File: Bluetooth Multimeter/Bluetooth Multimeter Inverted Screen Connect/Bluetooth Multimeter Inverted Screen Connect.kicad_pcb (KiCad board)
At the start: 2 copper layers, 55 x 90 mm, 33 parts, among them J1 V/Ohm, J2 Com, J3 mA, J4 A, J5 Parallel Prot, J6 3.3V, J7 GND, K1 Low Range, K2 Medium Range, K3 High Range, K4 UH Range (Ohm Only), K5 V/Ohm Switch, U1 ItsyBitsy_NRF52840_Big

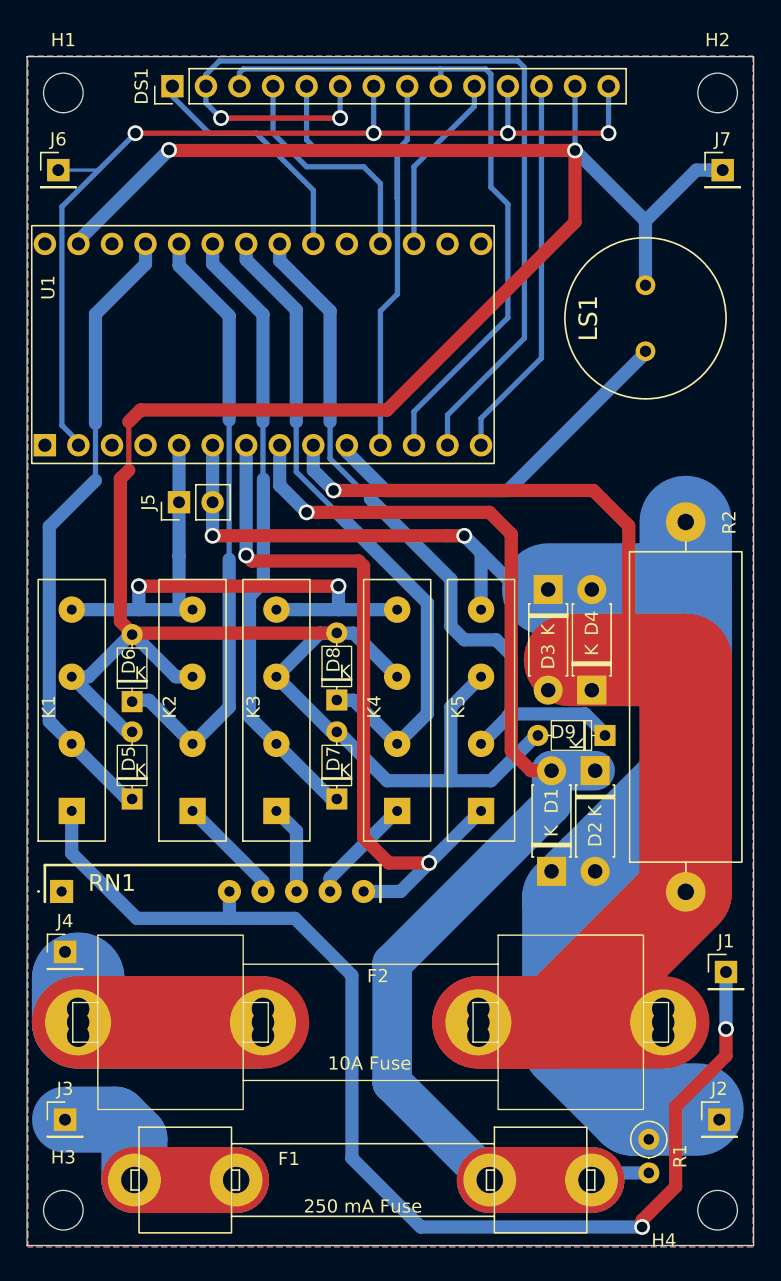
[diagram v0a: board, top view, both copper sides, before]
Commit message: began work on inverted screen connect project
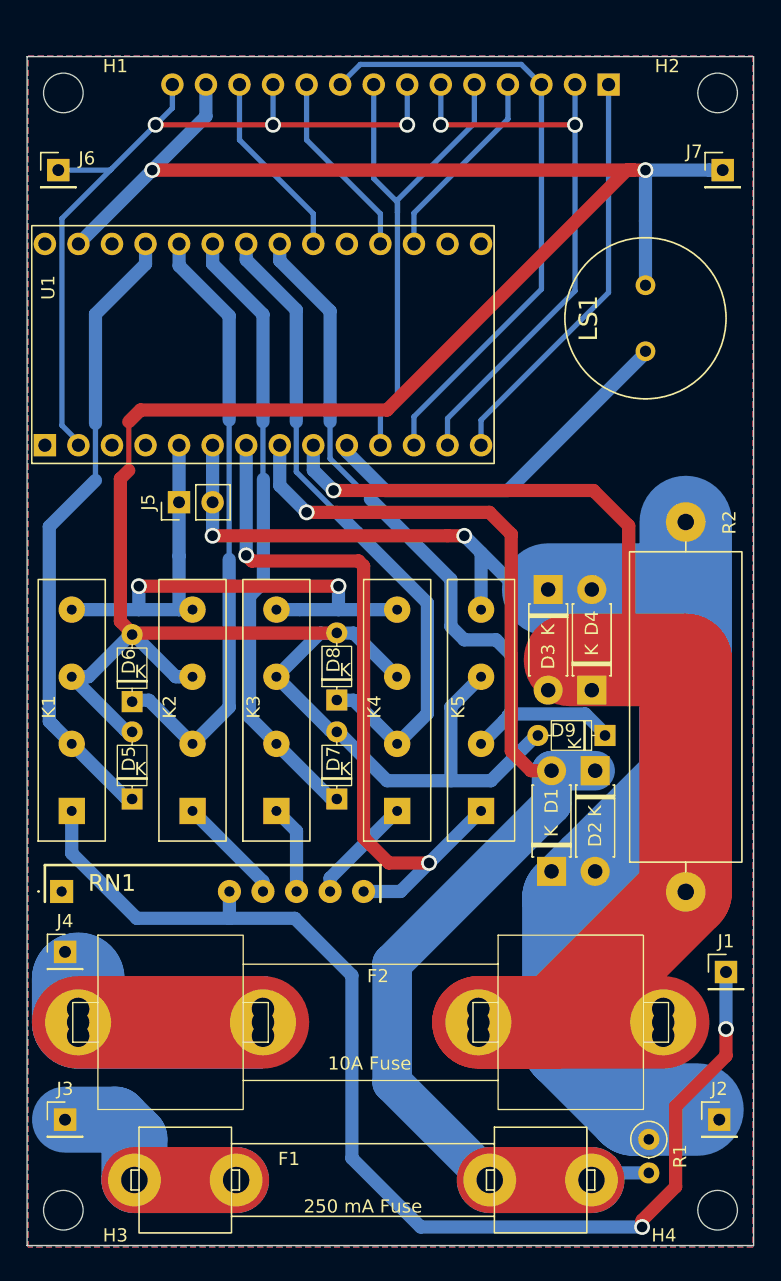
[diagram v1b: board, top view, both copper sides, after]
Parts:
- DS1: moved to B.Cu
- moved DS1 33.0 mm to (164.3, 55.5)
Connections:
- U1 pad 14: /TFT CS -> /TOUCH IRQ
- U1 pad 17: /TFT DC -> /TOUCH CS
- U1 pad 18: /TOUCH CS -> /TFT DC
- U1 pad 20: /TOUCH IRQ -> /TFT CS
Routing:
- net /MISO: track 70.7 -> 44.5 mm
- net /TOUCH IRQ: track 17.4 -> 31.3 mm
- net /TFT CS: track 28.1 -> 14.4 mm
- net +3.3V: track 73.4 -> 60.2 mm, vias 4 -> 3
- net /MOSI: track 52.9 -> 47.8 mm
- net GND: track 210.6 -> 214.9 mm
- net /TOUCH CS: track 17.8 -> 15.0 mm
- net /TFT DC: track 12.8 -> 14.4 mm
